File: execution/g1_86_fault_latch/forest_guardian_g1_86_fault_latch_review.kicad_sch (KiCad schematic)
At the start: 112 parts, among them J1 REVIEW_B77_J_ARM_REQ, J10 REVIEW_B78_J_MCU_G7, J11 REVIEW_B78_J_MODULE_G1, J12 REVIEW_B78_J_MODULE_G2, J13 REVIEW_B78_J_MODULE_G3, J14 REVIEW_B78_J_MODULE_G4, J15 REVIEW_B78_J_MODULE_G5, J16 REVIEW_B78_J_MODULE_G6, J17 REVIEW_B78_J_MODULE_G7, J18 UNQUALIFIED FAULT CLEAR, J2 REVIEW_B77_J_REARM, J3 REVIEW_B77_J_STOP, J4 REVIEW_B78_J_MCU_G1, J5 REVIEW_B78_J_MCU_G2, J6 REVIEW_B78_J_MCU_G3, J7 REVIEW_B78_J_MCU_G4, J8 REVIEW_B78_J_MCU_G5, J9 REVIEW_B78_J_MCU_G6, U1 REVIEW_B77_U_5V, U10 REVIEW_B77_U_RELEASE_FF, U11 REVIEW_B77_U_RELEASE_INV, U12 REVIEW_B77_U_RUN, U13 REVIEW_B77_U_WD, U14 TPS259474LRPW, U15 REVIEW_B78_U_BUF1, U16 REVIEW_B78_U_BUF2, U17 REVIEW_B78_U_BUF3, U18 REVIEW_B78_U_BUF4, U19 REVIEW_B81_U_RAIL_SV, U2 REVIEW_B77_U_ARM, U20 SN74LVC2G02DCUR, U21 SN74LVC1G04DBVR, U22 SN74LVC1G08DBVR, U3 REVIEW_B77_U_ARM_AND, U4 REVIEW_B77_U_ARM_INV, U5 REVIEW_B77_U_D_FINAL_AND, U6 REVIEW_B77_U_EDGE, U7 REVIEW_B77_U_HB_INV, U8 REVIEW_B77_U_POR, U9 REVIEW_B77_U_REARM_SCH

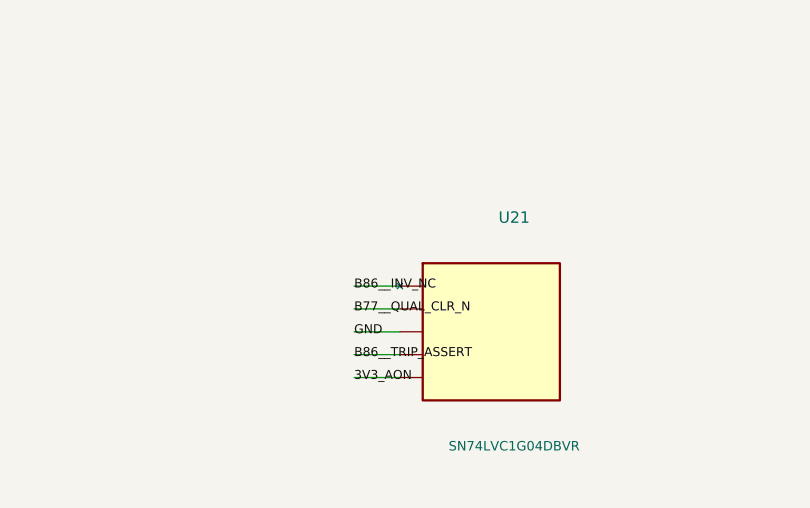
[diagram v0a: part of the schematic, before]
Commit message: G1-86: treat genuine TI inverter NC as native no-connect, preserve 404-pad netlist, fit all circuitry on review sheet
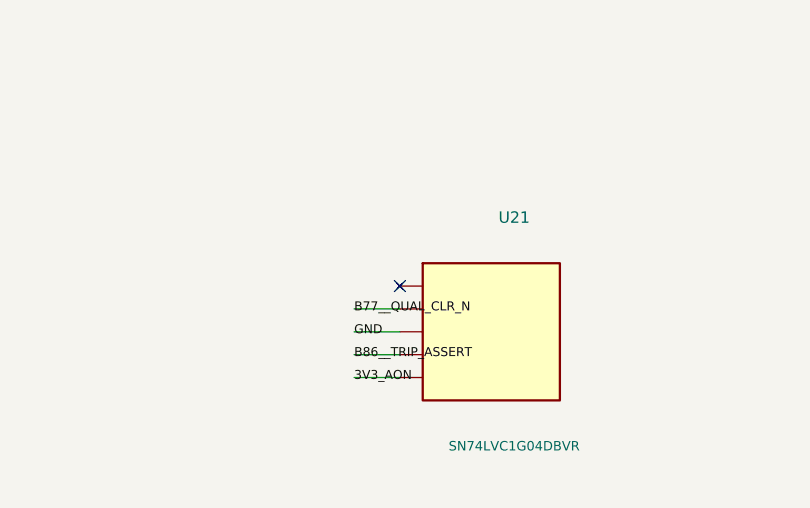
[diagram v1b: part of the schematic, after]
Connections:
- net B86__INV_NC: no longer names the net of U21.1 (NC)
- no-connect marks 0 -> 1
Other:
- title: Forest Guardian G1-85: TPS259474L pin 2/7/9/10 analog candidates (NO POWER) -> Forest Guardian G1-86: physical fault-priority NOR latch; NO MOTOR POWER
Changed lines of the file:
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@@
   (generator "forest_guardian_g1_86_fault_latch_review_export")
   (generator_version "1.0")
-  (paper "A0")
-  (title_block (title "Forest Guardian G1-85: TPS259474L pin 2/7/9/10 analog candidates (NO POWER)") (date "2026-10-16") (rev "G1-86 HOLD") (comment 1 "IN_BOM=no / ON_BOARD=no: ABSTRACT PIN SYMBOLS, NOT REAL FOOTPRINTS") (comment 2 "MOTOR EFUSE EN to GND, ALL 28 PHASE BUFFERS DISABLED") (comment 3 "No PCB, KiCad CLI ERC, HIL, or production release"))
+  (paper "User" 1200 1000)
+  (title_block (title "Forest Guardian G1-86: physical fault-priority NOR latch; NO MOTOR POWER") (date "2026-10-16") (rev "G1-86 HOLD") (comment 1 "IN_BOM=no / ON_BOARD=no: ABSTRACT PIN SYMBOLS, NOT REAL FOOTPRINTS") (comment 2 "MOTOR EFUSE EN to GND, ALL 28 PHASE BUFFERS DISABLED") (comment 3 "No PCB, KiCad CLI ERC, HIL, or production release"))
   (wire (pts (xy 48.26 59.69) (xy 53.34 59.69)) (stroke (width 0) (type default)))
   (wire (pts (xy 48.26 62.23) (xy 53.34 62.23)) (stroke (width 0) (type default)))
@@
   (wire (pts (xy 48.26 887.73) (xy 53.34 887.73)) (stroke (width 0) (type default)))
   (wire (pts (xy 48.26 890.27) (xy 53.34 890.27)) (stroke (width 0) (type default)))
-  (wire (pts (xy 160.02 876.3) (xy 165.1 876.3)) (stroke (width 0) (type default)))
   (wire (pts (xy 160.02 878.84) (xy 165.1 878.84)) (stroke (width 0) (type default)))
   (wire (pts (xy 160.02 881.38) (xy 165.1 881.38)) (stroke (width 0) (type default)))
@@
   (label "B86__FAULT_Q" (at 48.26 887.73 0) (effects (font (size 1 1))))
   (label "3V3_AON" (at 48.26 890.27 0) (effects (font (size 1 1))))
-  (label "B86__INV_NC" (at 160.02 876.3 0) (effects (font (size 1 1))))
   (label "B77__QUAL_CLR_N" (at 160.02 878.84 0) (effects (font (size 1 1))))
   (label "GND" (at 160.02 881.38 0) (effects (font (size 1 1))))
@@
     (instances (project "forest_guardian_g1_86_fault_latch_review" (path "/6c498f0d-d858-4eaa-adb9-b8d5e4383e8a" (reference "R54") (unit 1))))
   )
+  (no_connect (at 165.1 876.3))
   (sheet_instances (path "/" (page "1")))
 )
